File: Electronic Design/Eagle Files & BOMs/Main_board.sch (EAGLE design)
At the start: 38 parts, among them IC2 ATMEGA328-PU, IC3 LM2576S, Q1 IRF9540, Q2 IRF9540, X1 16MHz

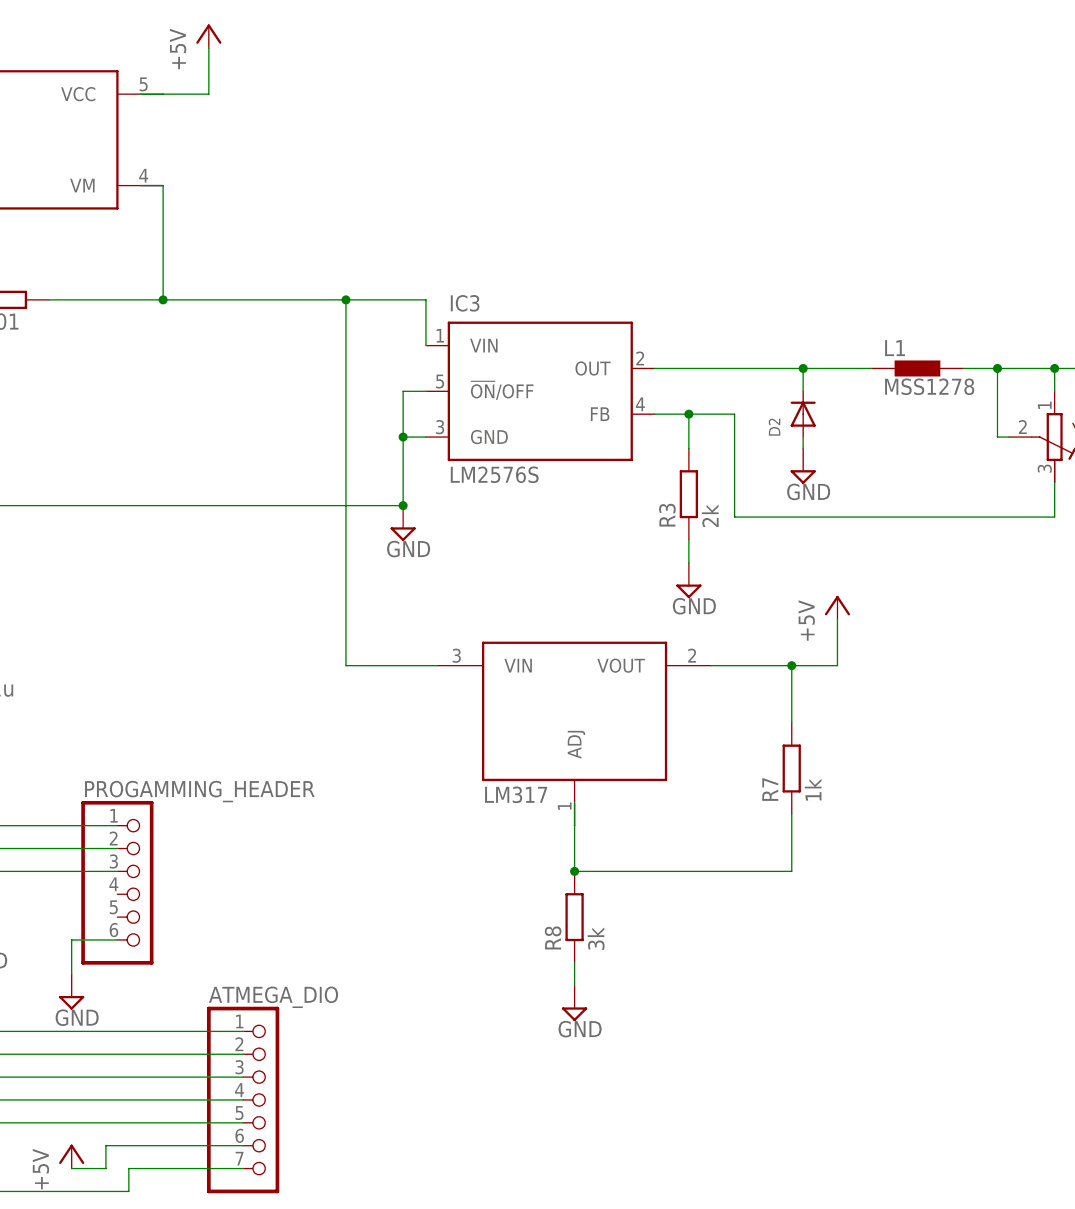
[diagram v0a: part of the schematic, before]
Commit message: addig smoothing caps for LM317 out and CS80 inputs
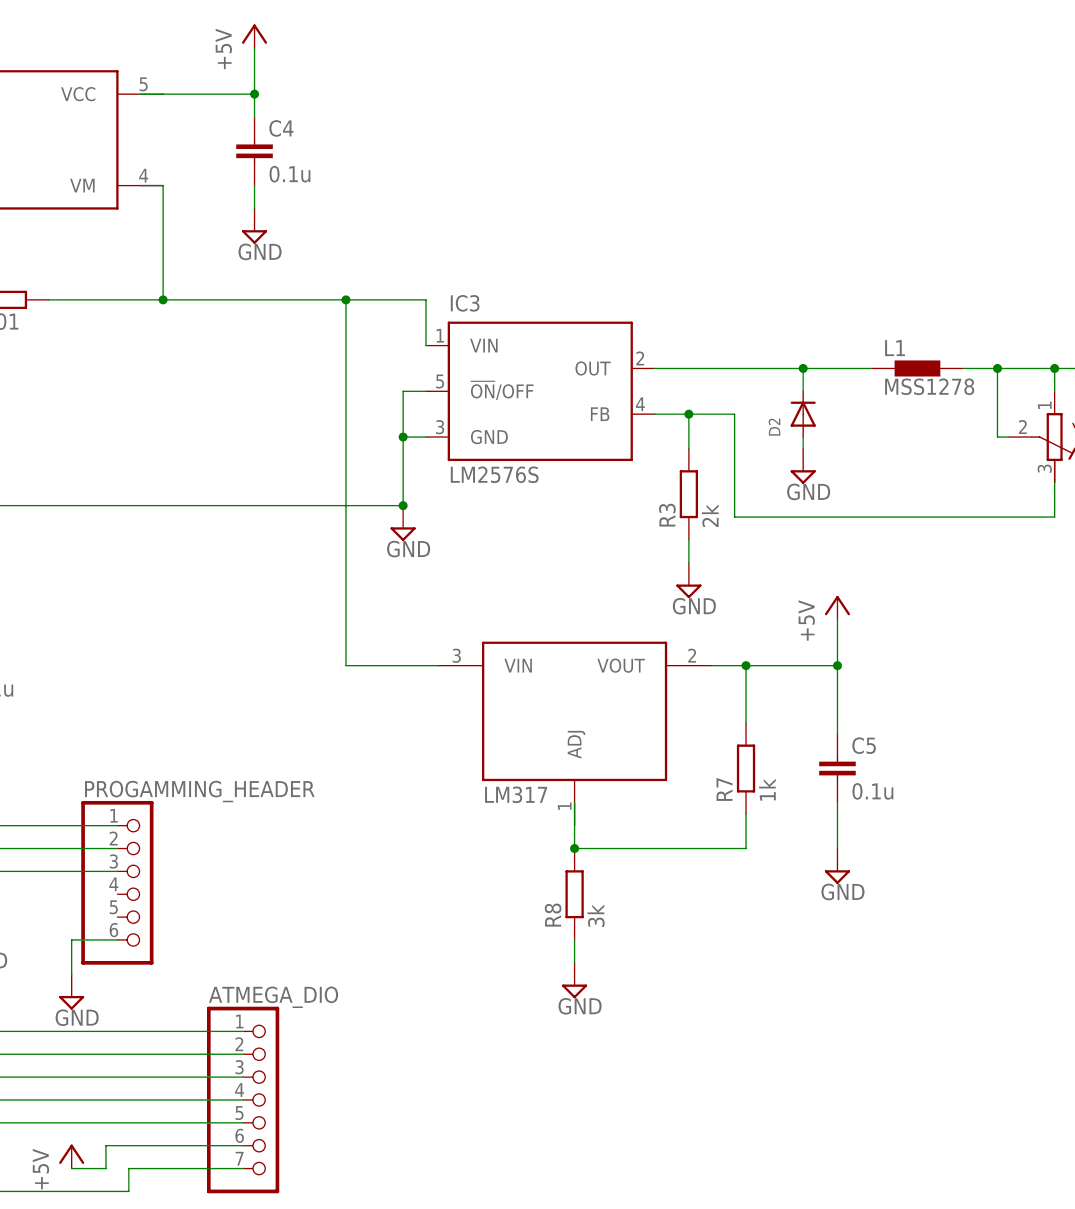
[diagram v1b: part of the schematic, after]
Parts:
- added C4, C5: 0.1u, resistor:C-EUC1206K
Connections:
- net +5V: now also C4.1, C5.1
- net GND: now also C4.2, C5.2
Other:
- moved on the sheet: R7, R8

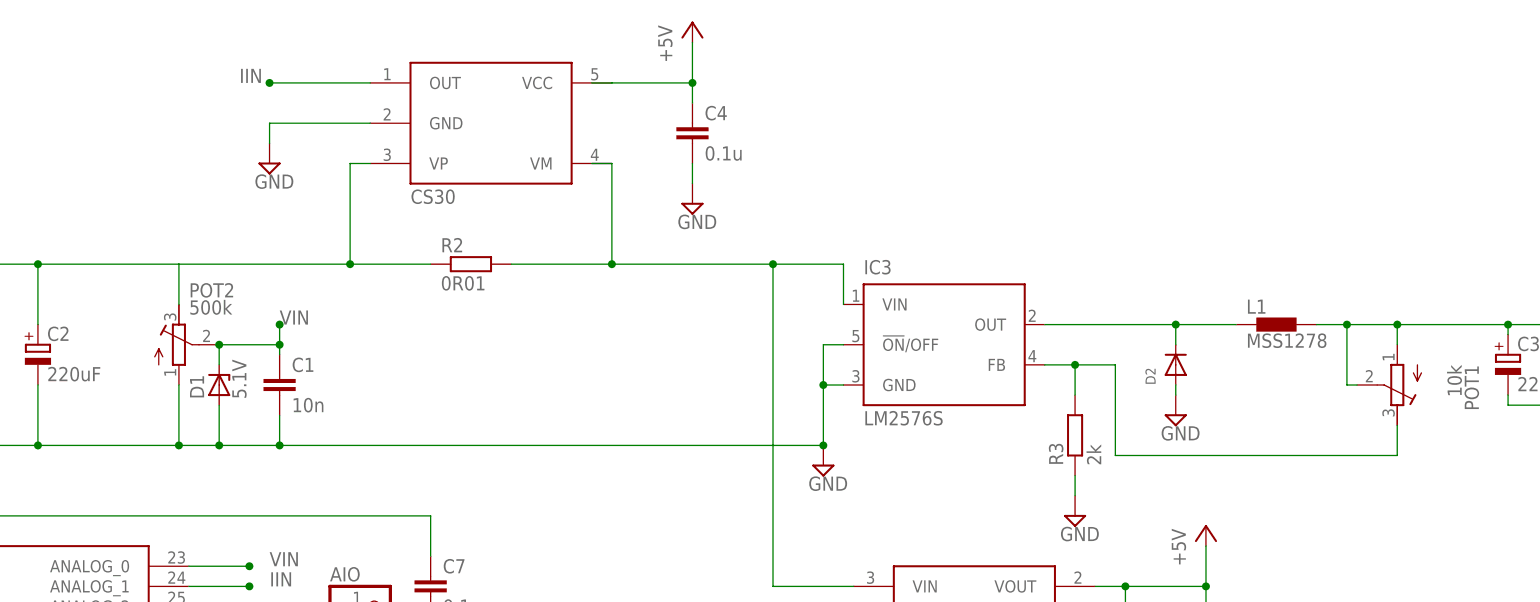
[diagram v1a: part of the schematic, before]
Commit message: adding smoothing caps and zeners to Iin
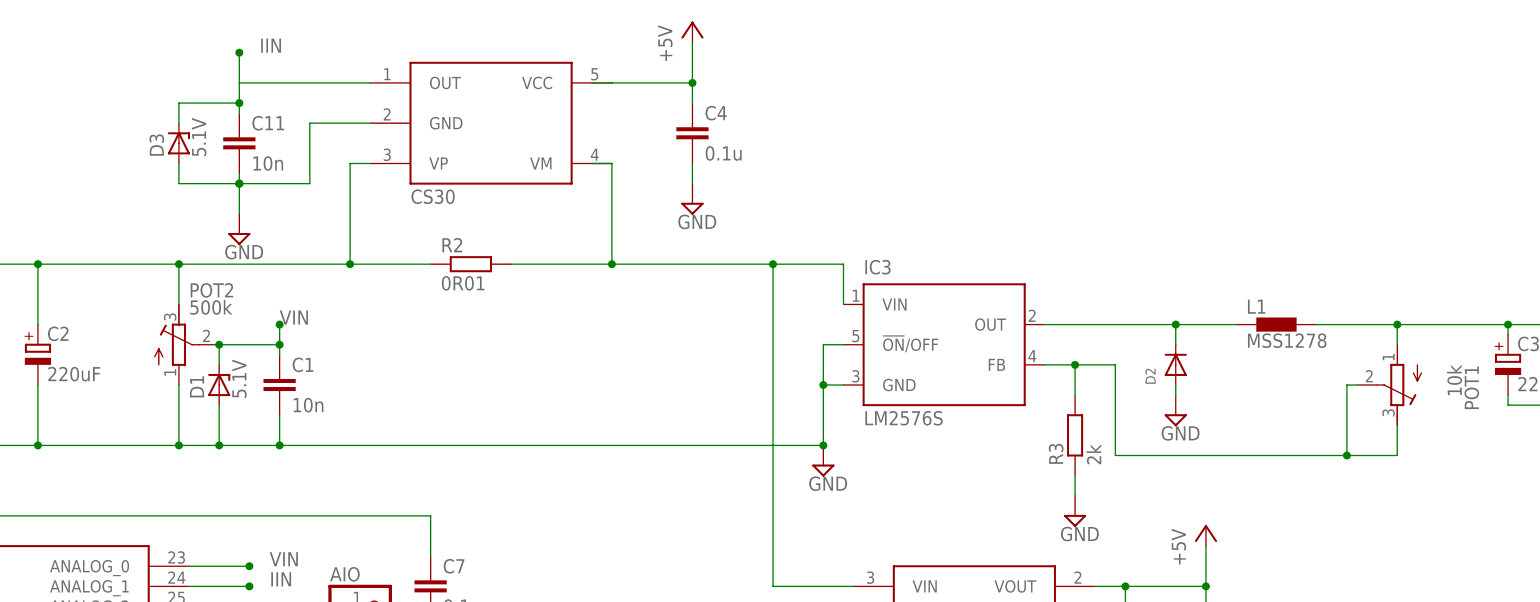
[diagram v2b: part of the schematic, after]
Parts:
- added C11: 10n, resistor:C-EUC1206K
- added D3: 5.1V, diode:ZPD
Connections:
- removed net N$2: IC3.FB, POT1.E, R3.2
- new net N$26: IC3.FB, POT1.E, POT1.S, R3.2
- net GND: now also C11.2, D3.A
- net IIN: now also C11.1, D3.C
- net N$24: no longer POT1.S
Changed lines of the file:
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@@
 <part name="SUPPLY10" library="supply2" deviceset="GND" device=""/>
 <part name="SUPPLY11" library="supply2" deviceset="GND" device=""/>
+<part name="C11" library="resistor" deviceset="C-EU" device="C1206K" value="10n"/>
+<part name="D3" library="diode" deviceset="ZPD" device="" value="5.1V"/>
 </parts>
 <sheets>
@@
 <instance part="R2" gate="G$1" x="22.86" y="88.9"/>
 <instance part="+3V2" gate="1" x="50.8" y="119.38"/>
-<instance part="SUPPLY1" gate="GND" x="-2.54" y="101.6"/>
+<instance part="SUPPLY1" gate="GND" x="-6.35" y="92.71"/>
 <instance part="IC3" gate="G$1" x="82.55" y="78.74"/>
 <instance part="SUPPLY7" gate="GND" x="67.31" y="63.5"/>
@@
 <instance part="SUPPLY10" gate="GND" x="50.8" y="96.52"/>
 <instance part="SUPPLY11" gate="GND" x="115.57" y="25.4"/>
+<instance part="C11" gate="G$1" x="-6.35" y="105.41"/>
+<instance part="D3" gate="G$1" x="-13.97" y="104.14" rot="R90"/>
 </instances>
 <busses>
@@
 </segment>
 <segment>
-<wire x1="10.16" y1="111.76" x2="-2.54" y2="111.76" width="0.1524" layer="91"/>
-<junction x="-2.54" y="111.76"/>
-<label x="-6.35" y="111.76" size="1.778" layer="95"/>
+<wire x1="10.16" y1="111.76" x2="-6.35" y2="111.76" width="0.1524" layer="91"/>
+<junction x="-6.35" y="115.57"/>
+<label x="-3.81" y="115.57" size="1.778" layer="95"/>
 <pinref part="U$2" gate="G$1" pin="OUT"/>
+<pinref part="C11" gate="G$1" pin="1"/>
+<wire x1="-6.35" y1="111.76" x2="-6.35" y2="115.57" width="0.1524" layer="91"/>
+<wire x1="-6.35" y1="111.76" x2="-6.35" y2="109.22" width="0.1524" layer="91"/>
+<pinref part="D3" gate="G$1" pin="C"/>
+<wire x1="-6.35" y1="109.22" x2="-6.35" y2="107.95" width="0.1524" layer="91"/>
+<wire x1="-13.97" y1="106.68" x2="-13.97" y2="109.22" width="0.1524" layer="91"/>
+<wire x1="-13.97" y1="109.22" x2="-6.35" y2="109.22" width="0.1524" layer="91"/>
+<junction x="-6.35" y="109.22"/>
 </segment>
 </net>
@@
 </segment>
 <segment>
-<wire x1="10.16" y1="106.68" x2="-2.54" y2="106.68" width="0.1524" layer="91"/>
-<wire x1="-2.54" y1="106.68" x2="-2.54" y2="104.14" width="0.1524" layer="91"/>
 <pinref part="SUPPLY1" gate="GND" pin="GND"/>
+<pinref part="C11" gate="G$1" pin="2"/>
+<wire x1="-6.35" y1="99.06" x2="-6.35" y2="95.25" width="0.1524" layer="91"/>
+<wire x1="-6.35" y1="100.33" x2="-6.35" y2="99.06" width="0.1524" layer="91"/>
+<pinref part="D3" gate="G$1" pin="A"/>
+<wire x1="-13.97" y1="101.6" x2="-13.97" y2="99.06" width="0.1524" layer="91"/>
+<wire x1="-13.97" y1="99.06" x2="-6.35" y2="99.06" width="0.1524" layer="91"/>
+<junction x="-6.35" y="99.06"/>
+<junction x="-6.35" y="99.06"/>
 <pinref part="U$2" gate="G$1" pin="GND"/>
+<wire x1="10.16" y1="106.68" x2="2.54" y2="106.68" width="0.1524" layer="91"/>
+<wire x1="2.54" y1="106.68" x2="2.54" y2="99.06" width="0.1524" layer="91"/>
+<wire x1="2.54" y1="99.06" x2="-6.35" y2="99.06" width="0.1524" layer="91"/>
 </segment>
 <segment>
@@
 <junction x="7.62" y="88.9"/>
 <pinref part="U$2" gate="G$1" pin="VP"/>
+<junction x="-13.97" y="88.9"/>
 </segment>
 </net>
@@
 </segment>
 </net>
-<net name="N$2" class="0">
-<segment>
+<net name="N$24" class="0">
+<segment>
+<pinref part="L1" gate="G$1" pin="2"/>
+<pinref part="POT1" gate="G$1" pin="A"/>
+<wire x1="129.54" y1="81.28" x2="139.7" y2="81.28" width="0.1524" layer="91"/>
+<wire x1="139.7" y1="81.28" x2="139.7" y2="78.74" width="0.1524" layer="91"/>
+<pinref part="C3" gate="G$1" pin="+"/>
+<wire x1="139.7" y1="81.28" x2="153.67" y2="81.28" width="0.1524" layer="91"/>
+<wire x1="153.67" y1="81.28" x2="153.67" y2="80.01" width="0.1524" layer="91"/>
+<pinref part="VOUT" gate="A" pin="1"/>
+<wire x1="153.67" y1="81.28" x2="168.91" y2="81.28" width="0.1524" layer="91"/>
+<junction x="153.67" y="81.28"/>
+<junction x="139.7" y="81.28"/>
+</segment>
+</net>
+<net name="N$26" class="0">
+<segment>
+<pinref part="POT1" gate="G$1" pin="S"/>
+<wire x1="133.35" y1="73.66" x2="134.62" y2="73.66" width="0.1524" layer="91"/>
 <pinref part="IC3" gate="G$1" pin="FB"/>
 <pinref part="R3" gate="G$1" pin="2"/>
@@
 <pinref part="POT1" gate="G$1" pin="E"/>
 <wire x1="139.7" y1="68.58" x2="139.7" y2="64.77" width="0.1524" layer="91"/>
-<wire x1="139.7" y1="64.77" x2="104.14" y2="64.77" width="0.1524" layer="91"/>
+<wire x1="139.7" y1="64.77" x2="133.35" y2="64.77" width="0.1524" layer="91"/>
 <junction x="99.06" y="76.2"/>
-</segment>
-</net>
-<net name="N$24" class="0">
-<segment>
-<pinref part="L1" gate="G$1" pin="2"/>
-<pinref part="POT1" gate="G$1" pin="A"/>
-<wire x1="129.54" y1="81.28" x2="133.35" y2="81.28" width="0.1524" layer="91"/>
-<wire x1="133.35" y1="81.28" x2="139.7" y2="81.28" width="0.1524" layer="91"/>
-<wire x1="139.7" y1="81.28" x2="139.7" y2="78.74" width="0.1524" layer="91"/>
-<pinref part="POT1" gate="G$1" pin="S"/>
-<wire x1="133.35" y1="81.28" x2="133.35" y2="73.66" width="0.1524" layer="91"/>
-<wire x1="133.35" y1="73.66" x2="134.62" y2="73.66" width="0.1524" layer="91"/>
-<junction x="133.35" y="81.28"/>
-<pinref part="C3" gate="G$1" pin="+"/>
-<wire x1="139.7" y1="81.28" x2="153.67" y2="81.28" width="0.1524" layer="91"/>
-<wire x1="153.67" y1="81.28" x2="153.67" y2="80.01" width="0.1524" layer="91"/>
-<pinref part="VOUT" gate="A" pin="1"/>
-<wire x1="153.67" y1="81.28" x2="168.91" y2="81.28" width="0.1524" layer="91"/>
-<junction x="153.67" y="81.28"/>
-<junction x="139.7" y="81.28"/>
-</segment>
-</net>
+<wire x1="133.35" y1="64.77" x2="104.14" y2="64.77" width="0.1524" layer="91"/>
+<wire x1="133.35" y1="73.66" x2="133.35" y2="64.77" width="0.1524" layer="91"/>
+<junction x="133.35" y="64.77"/>
+</segment>
+</net>
